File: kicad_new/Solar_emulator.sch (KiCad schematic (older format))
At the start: 1 part

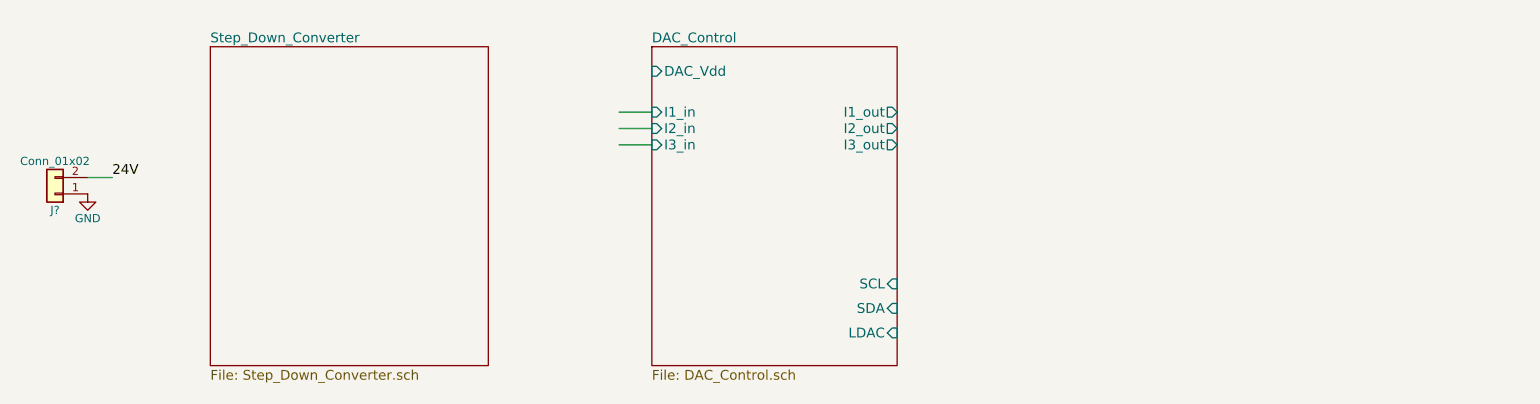
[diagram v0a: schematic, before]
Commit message: Added INA's and connectors
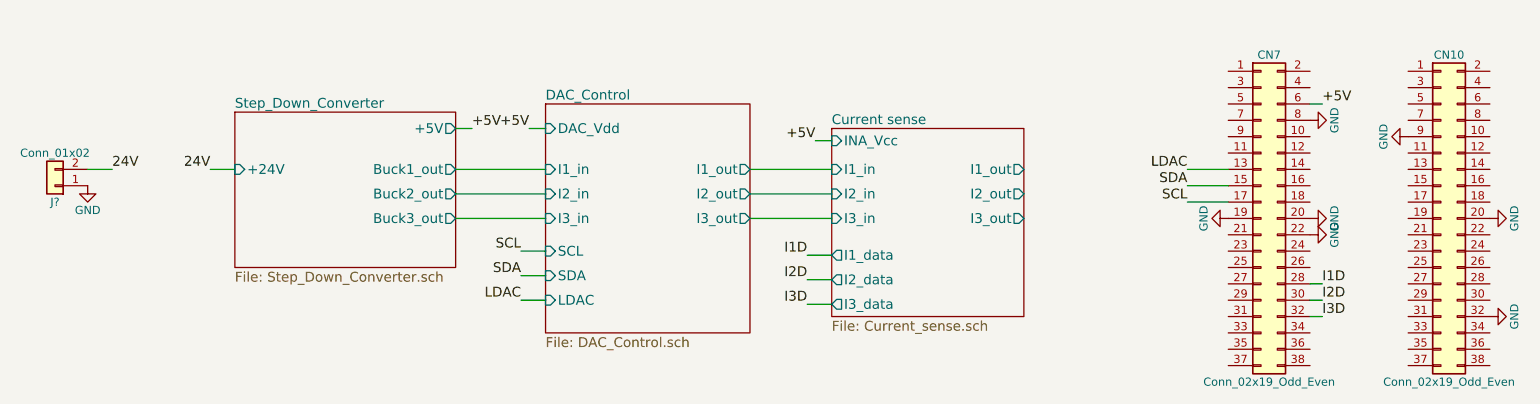
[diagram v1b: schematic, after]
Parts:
- added CN10, CN7: Conn_02x19_Odd_Even, symbol Conn_02x19_Odd_Even
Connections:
- net labels added: +5V, I1D, I2D, I3D, LDAC, SCL, SDA
- wire segments 4 -> 24
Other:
- moved on the sheet: J?

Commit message: Added a text
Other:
- note added: "For Nucleo-F334R8"
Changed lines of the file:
@@
 Text Label 7975 4200 2    60   ~ 0
 LDAC
+Text Notes 8575 3350 0    60   ~ 0
+For Nucleo-F334R8
 $EndSCHEMATC
